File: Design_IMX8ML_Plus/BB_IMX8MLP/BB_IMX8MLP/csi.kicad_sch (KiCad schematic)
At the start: 33 parts, among them J12 CAM_1, J13 CAM_2, U23 D3V3F4U10LP-7, U44 D3V3F4U10LP-7, U45 FXMA2102L8X, U47 D3V3F4U10LP-7, U48 D3V3F4U10LP-7, U51 FXMA2102L8X

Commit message: [LoRa] Starting a new project
Starting a new project base on LoRa LR1121, this project use
the module LBAA0XV2GT-001 that had sub-GHz and 2.4GHz frequencies.
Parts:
- J12: footprint Connector_FFC-FPC:Hirose_FH12-24S-0.5SH_1x24-1MP_P0.50mm_Horizontal -> _W_SBC:687124182122; MP (none) -> 687124182122; Price (none) -> 2
- J13: footprint Connector_FFC-FPC:Hirose_FH12-24S-0.5SH_1x24-1MP_P0.50mm_Horizontal -> _W_SBC:687124182122; MP (none) -> FH12-24S-0.5SVA(54); Price (none) -> 2
- L10, L11, L12, L13, L14, L15, L16, L7, L8, L9: MP (none) -> EXC-14CH120U; Price (none) -> 0.3
- U19, U46: value ~ -> D3V3F4U10LP-7; MP (none) -> D3V3F4U10LP-7; Price (none) -> 0.35
- U53: value ~ -> SN74AVC4T774RSVR; footprint (none) -> Package_DFN_QFN:UQFN-16_1.8x2.6mm_P0.4mm; MP (none) -> SN74AVC4T774RSVR; Price (none) -> 2
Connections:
- net GND: now also U19.3 (GND), U19.8 (GND), U23.3 (GND), U23.8 (GND), U44.3 (GND), U44.8 (GND), U46.3 (GND), U46.8 (GND), U47.3 (GND), U47.8 (GND), U48.3 (GND), U48.8 (GND)
- no-connect marks 2 -> 6
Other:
- moved on the sheet: L12, L13, L16, U46, U48

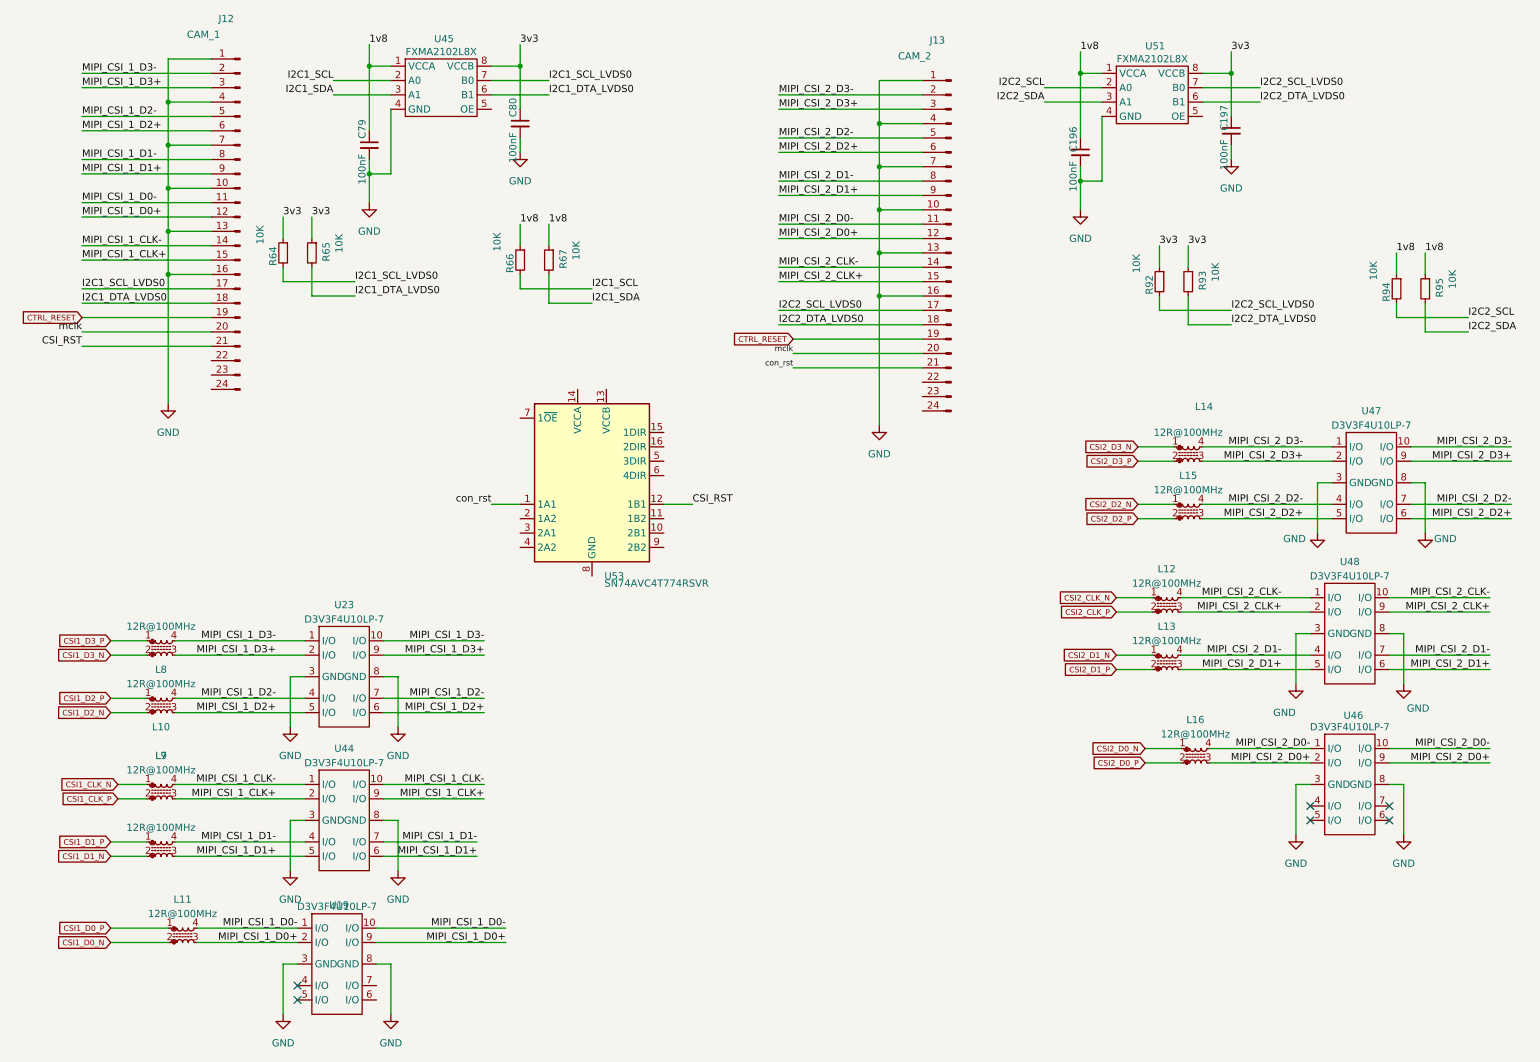
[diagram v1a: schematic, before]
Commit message: [BB_IMX8ML] It was reoganizated the device position
It was reorganized the devices to improve the routing.
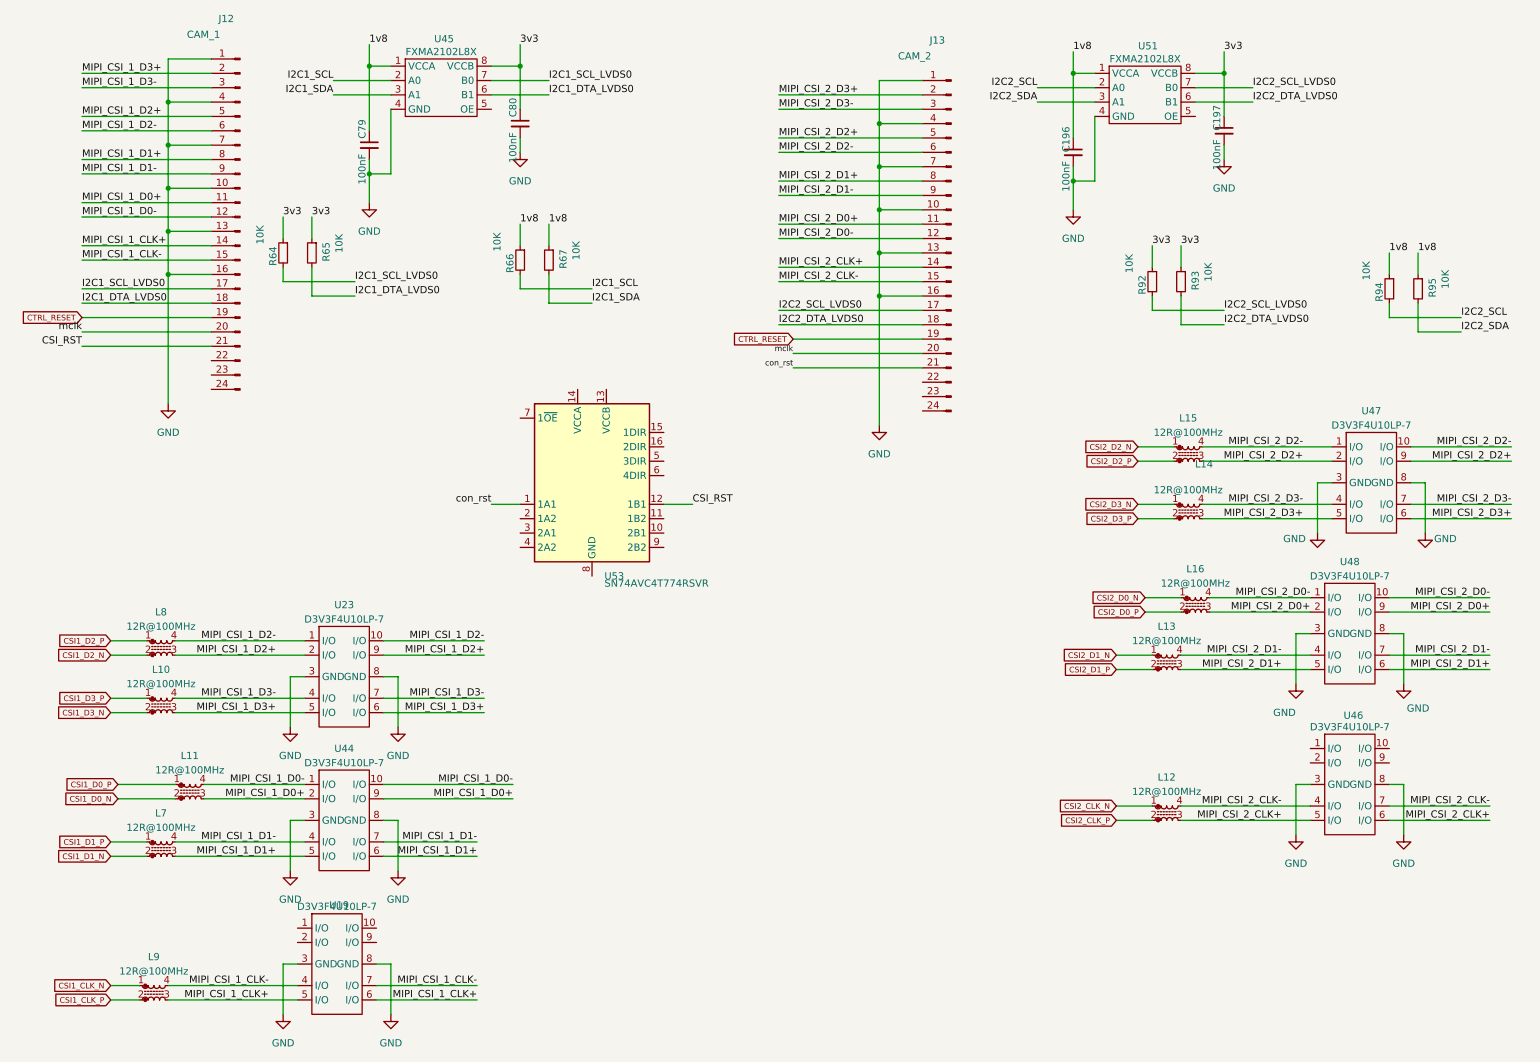
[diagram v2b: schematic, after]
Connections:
- net MIPI_CSI_1_CLK+: now also J12.14 (Pin_14), U19.5 (I/O), U19.6 (I/O); no longer J12.15 (Pin_15), U44.2 (I/O), U44.9 (I/O)
- net MIPI_CSI_1_CLK-: now also J12.15 (Pin_15), U19.4 (I/O), U19.7 (I/O); no longer J12.14 (Pin_14), U44.1 (I/O), U44.10 (I/O)
- net MIPI_CSI_1_D0+: now also J12.11 (Pin_11), U44.2 (I/O), U44.9 (I/O); no longer J12.12 (Pin_12), U19.2 (I/O), U19.9 (I/O)
- net MIPI_CSI_1_D0-: now also J12.12 (Pin_12), U44.1 (I/O), U44.10 (I/O); no longer J12.11 (Pin_11), U19.1 (I/O), U19.10 (I/O)
- net MIPI_CSI_1_D1+: now also J12.8 (Pin_8); no longer J12.9 (Pin_9)
- net MIPI_CSI_1_D1-: now also J12.9 (Pin_9); no longer J12.8 (Pin_8)
- net MIPI_CSI_1_D2+: now also J12.5 (Pin_5), U23.2 (I/O), U23.9 (I/O); no longer J12.6 (Pin_6), U23.5 (I/O), U23.6 (I/O)
- net MIPI_CSI_1_D2-: now also J12.6 (Pin_6), U23.1 (I/O), U23.10 (I/O); no longer J12.5 (Pin_5), U23.4 (I/O), U23.7 (I/O)
- net MIPI_CSI_1_D3+: now also J12.2 (Pin_2), U23.5 (I/O), U23.6 (I/O); no longer J12.3 (Pin_3), U23.2 (I/O), U23.9 (I/O)
- net MIPI_CSI_1_D3-: now also J12.3 (Pin_3), U23.4 (I/O), U23.7 (I/O); no longer J12.2 (Pin_2), U23.1 (I/O), U23.10 (I/O)
- net MIPI_CSI_2_CLK+: now also J13.14 (Pin_14), U46.5 (I/O), U46.6 (I/O); no longer J13.15 (Pin_15), U48.2 (I/O), U48.9 (I/O)
- net MIPI_CSI_2_CLK-: now also J13.15 (Pin_15), U46.4 (I/O), U46.7 (I/O); no longer J13.14 (Pin_14), U48.1 (I/O), U48.10 (I/O)
- net MIPI_CSI_2_D0+: now also J13.11 (Pin_11), U48.2 (I/O), U48.9 (I/O); no longer J13.12 (Pin_12), U46.2 (I/O), U46.9 (I/O)
- net MIPI_CSI_2_D0-: now also J13.12 (Pin_12), U48.1 (I/O), U48.10 (I/O); no longer J13.11 (Pin_11), U46.1 (I/O), U46.10 (I/O)
- net MIPI_CSI_2_D1+: now also J13.8 (Pin_8); no longer J13.9 (Pin_9)
- net MIPI_CSI_2_D1-: now also J13.9 (Pin_9); no longer J13.8 (Pin_8)
- net MIPI_CSI_2_D2+: now also J13.5 (Pin_5), U47.2 (I/O), U47.9 (I/O); no longer J13.6 (Pin_6), U47.5 (I/O), U47.6 (I/O)
- net MIPI_CSI_2_D2-: now also J13.6 (Pin_6), U47.1 (I/O), U47.10 (I/O); no longer J13.5 (Pin_5), U47.4 (I/O), U47.7 (I/O)
- net MIPI_CSI_2_D3+: now also J13.2 (Pin_2), U47.5 (I/O), U47.6 (I/O); no longer J13.3 (Pin_3), U47.2 (I/O), U47.9 (I/O)
- net MIPI_CSI_2_D3-: now also J13.3 (Pin_3), U47.4 (I/O), U47.7 (I/O); no longer J13.2 (Pin_2), U47.1 (I/O), U47.10 (I/O)
- no-connect marks 6 -> 0
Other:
- moved on the sheet: C196, C197, L11, L12, L14, L15, L16, L7, L8, L9, R92, R93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
